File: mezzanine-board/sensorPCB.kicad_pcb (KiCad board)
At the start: 2 copper layers, 55.5 x 19.8 mm, 21 parts, among them J1 90152-2140, U3 AS72652, U4 AS72653, U6 AS72651

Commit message: Add TE 215307-7 connector to mezzanine libraries
Import the Library Loader part (14-pin TE Connectivity connector) into
the mezzanine's already-registered SamacSys_Parts library: footprint, 3D
model, and symbol appended. 3D path rewritten to ${KIPRJMOD}-relative and
the symbol's Footprint property qualified with the library nickname.
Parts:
- removed J1: 90152-2140, SamacSys_Parts:901522140
- added J2: SSQ-120-04-G-D, SamacSys_Parts:SSQ-120-XX-YYY-D, F.Cu at (171.7, 92.0)
- moved U3 2.92 mm to (146.8, 83.2)
- moved U4 2.92 mm to (154.4, 83.2)
- moved U6 2.92 mm to (139.2, 83.2)
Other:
- board size 55.5 x 19.8 mm -> 55.5 x 16.6 mm

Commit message: Add Molex 90122-0770 right-angle header to main board libraries
Import the Library Loader part (2x10 right-angle header, 20-pin) into the
main board's SamacSys_Parts library: footprint, 3D model, and symbol
appended. 3D path rewritten to ${KIPRJMOD}-relative and the symbol's
Footprint property qualified with the library nickname.
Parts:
- moved U6 42.8 mm to (97.3, 91.6)
- moved U3 42.3 mm to (105.4, 91.7)
- moved U4 41.6 mm to (113.8, 91.9)
- moved J2 1.95 mm to (171.7, 94.0)
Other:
- board size 55.5 x 16.6 mm -> 82.1 x 13.6 mm
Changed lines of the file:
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@@
 	(footprint "SamacSys_Parts:AS72651BLGT"
 		(layer "F.Cu")
-		(at 146.791 83.165)
+		(at 105.41 91.694)
 		(descr "LGA-20")
 		(tags "Integrated Circuit")
@@
 	(footprint "SamacSys_Parts:SSQ-120-XX-YYY-D"
 		(layer "F.Cu")
-		(at 171.704 92.0295)
+		(at 171.704 93.98)
 		(descr "SSQ-120-XX-YYY-D")
 		(tags "Connector")
@@
 	(footprint "SamacSys_Parts:AS72651BLGT"
 		(layer "F.Cu")
-		(at 154.411 83.165)
+		(at 113.792 91.948)
 		(descr "LGA-20")
 		(tags "Integrated Circuit")
@@
 	(footprint "SamacSys_Parts:AS72651BLGT"
 		(layer "F.Cu")
-		(at 139.171 83.165)
+		(at 97.254 91.582)
 		(descr "LGA-20")
 		(tags "Integrated Circuit")
@@
 	)
 	(gr_rect
-		(start 119.834322 78.994)
+		(start 93.218 82.042)
 		(end 175.316821 95.60057)
 		(stroke

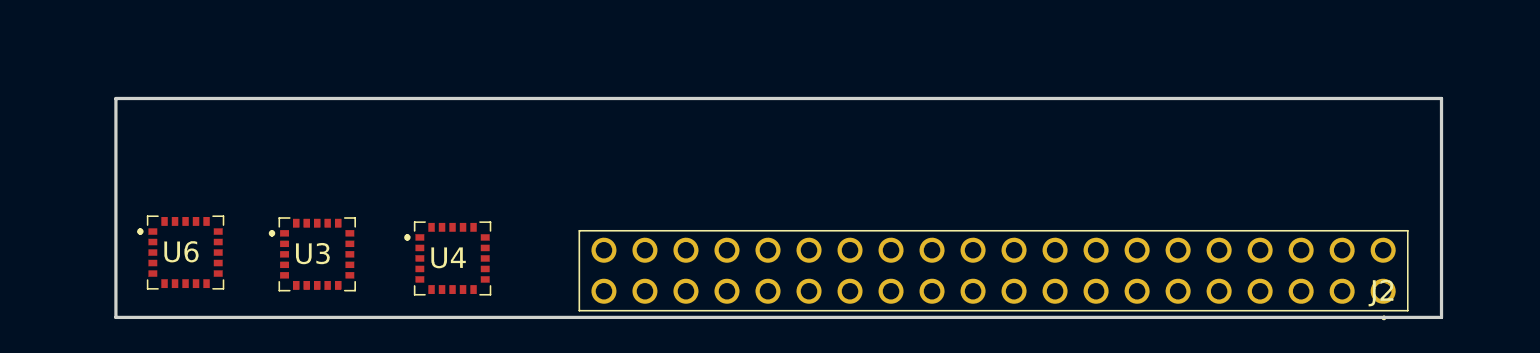
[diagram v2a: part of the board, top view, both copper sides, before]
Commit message: Add Samtec FTSH-110-01-F-D-RA header to mezzanine libraries
Import the Library Loader part (2x10 right-angle 1.27mm fine-pitch header)
into the mezzanine's SamacSys_Parts library: footprint, 3D model, and
symbol appended. 3D path rewritten to ${KIPRJMOD}-relative and the
symbol's Footprint property qualified with the library nickname.
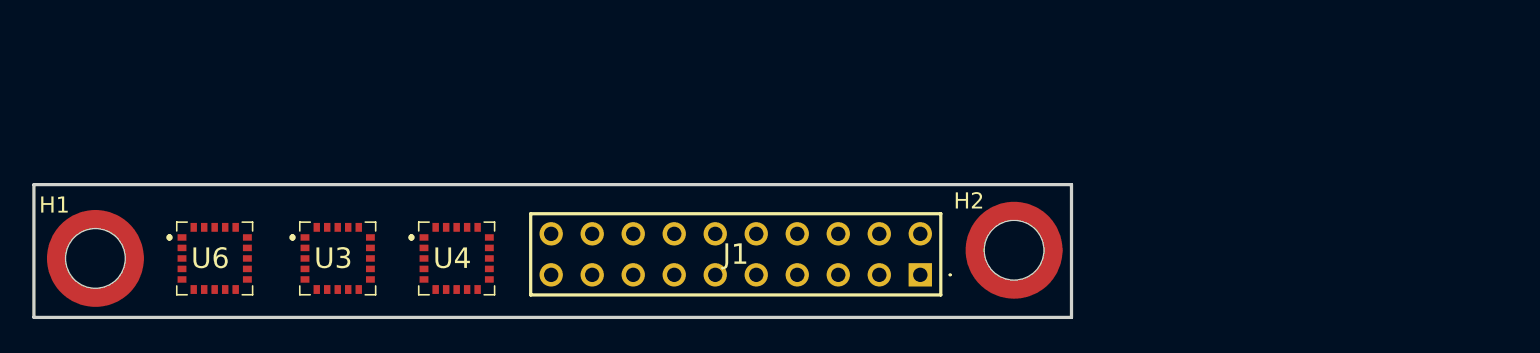
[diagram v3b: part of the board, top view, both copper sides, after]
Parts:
- removed J2: SSQ-120-04-G-D, SamacSys_Parts:SSQ-120-XX-YYY-D
- added H1: MountingHole, Mounting_Wuerth:Mounting_Wuerth_WA-SMSI-M2.5_H0.5mm_9774005151, F.Cu at (91.9, 91.9)
- added H2: MountingHole, Mounting_Wuerth:Mounting_Wuerth_WA-SMSI-M2.5_H0.5mm_9774005151, F.Cu at (148.8, 91.4)
- added J1: 1-534998-0, SamacSys_Parts:15349980, F.Cu at (143.0, 93.0)
- moved U6 1.84 mm to (99.1, 91.9)
- moved U3 1.30 mm to (106.7, 91.9)
- moved U4 0.25 mm to (114.0, 91.9)
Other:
- board size 82.1 x 13.6 mm -> 64.3 x 8.2 mm

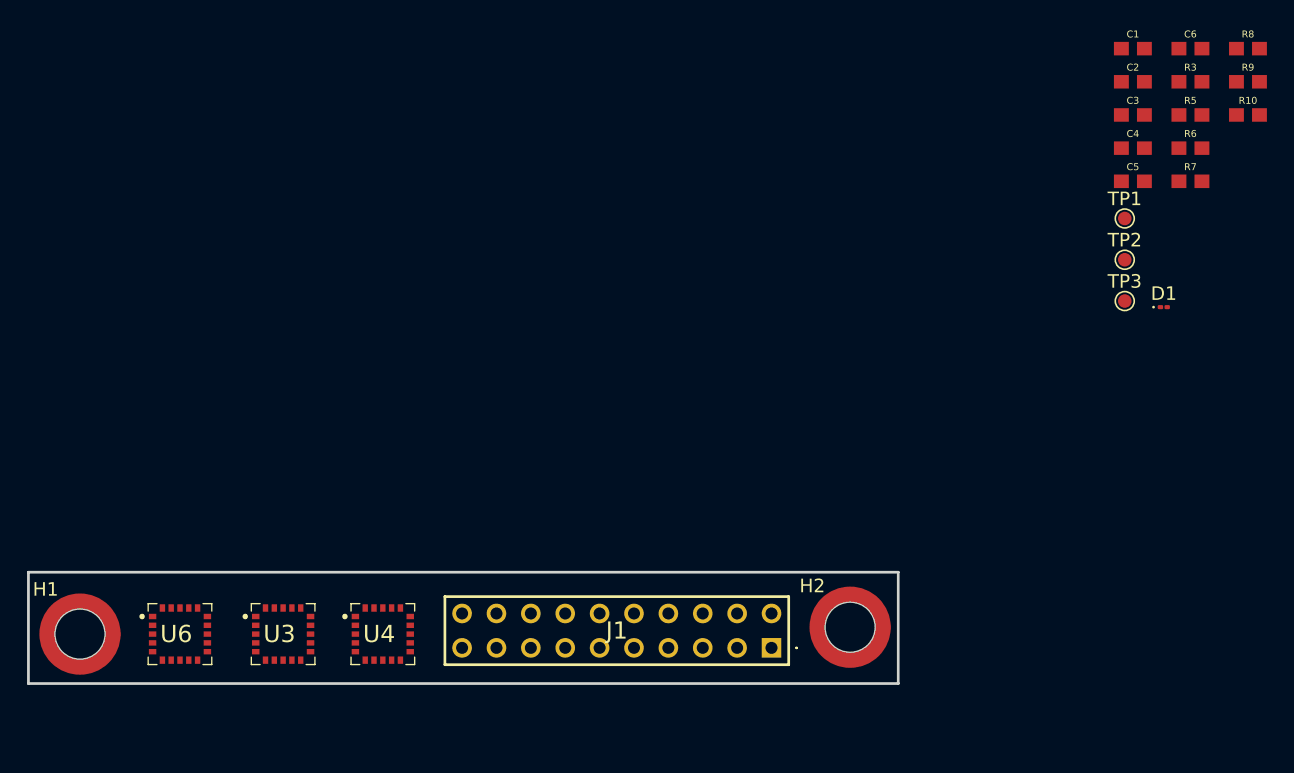
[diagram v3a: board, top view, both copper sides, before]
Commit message: Add Amphenol 20021311-00020T4LF (Minitek127) to mezzanine libraries
Import the Library Loader part (20-pin 1.27mm board-to-board connector)
into the mezzanine's SamacSys_Parts library: footprint, 3D model, and
symbol appended. 3D path rewritten to ${KIPRJMOD}-relative and the
symbol's Footprint property qualified with the library nickname.
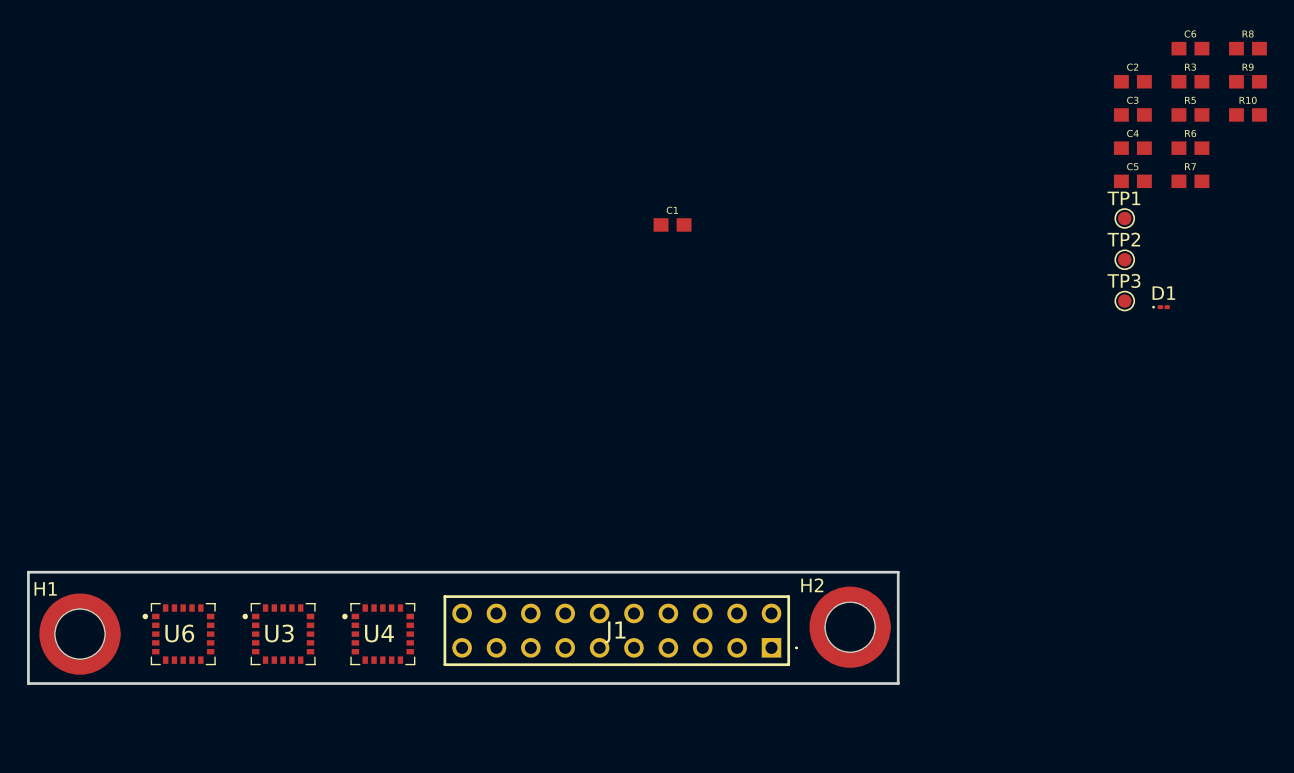
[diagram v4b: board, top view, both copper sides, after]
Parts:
- moved C1 36.4 mm to (135.7, 61.7)
- moved U6 0.24 mm to (99.3, 91.9)
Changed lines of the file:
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@@
 		(model "${KIPRJMOD}/libraries/3dmodels/SamacSys_Parts.3dshapes/1-534998-0.stp"
 			(offset
-				(xyz -11.43000013 1.269999962 0.4900000022)
+				(xyz -11.43 1.27 -1.51)
 			)
 			(scale
@@
 			)
 			(rotate
-				(xyz 0 0 0)
+				(xyz -0 -180 -0)
 			)
 		)
@@
 	(footprint "SamacSys_Parts:AS72651BLGT"
 		(layer "F.Cu")
-		(at 99.06 91.948)
+		(at 99.3 91.948)
 		(descr "LGA-20")
 		(tags "Integrated Circuit")
@@
 	(footprint "SparkfunLibrary:0603"
 		(layer "F.Cu")
-		(at 169.7343 48.6933)
+		(at 135.724 61.722)
 		(descr "Generic 1608 (0603) package\n\n0.2mm courtyard excess rounded to nearest 0.05mm.")
 		(property "Reference" "C1"

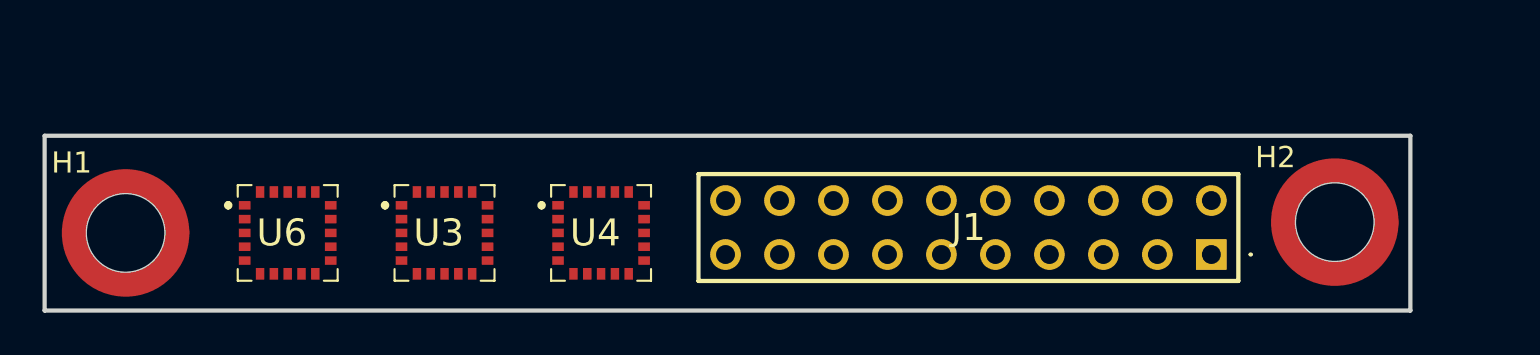
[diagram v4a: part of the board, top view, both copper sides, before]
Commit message: Add Samtec FTSH-110-01-F-D-RA header to main board libraries
Import the Library Loader part (2x10 right-angle 1.27mm fine-pitch header)
into the main board's SamacSys_Parts library: footprint, 3D model, and
symbol appended. 3D path rewritten to ${KIPRJMOD}-relative and the
symbol's Footprint property qualified with the library nickname.
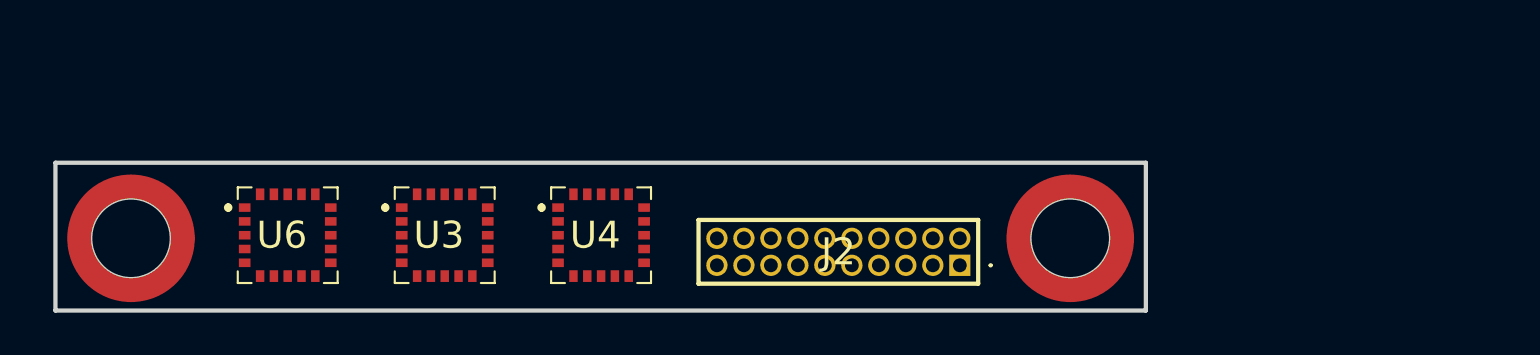
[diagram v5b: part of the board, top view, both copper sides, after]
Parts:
- removed J1: 1-534998-0, SamacSys_Parts:15349980
- added J2: 20021311-00020T4LF, SamacSys_Parts:2002131100020T4LF, F.Cu at (131.2, 93.5)
- moved H2 12.5 mm to (136.4, 92.2)
- moved H1 0.36 mm to (92.2, 92.2)
- moved U3 0.11 mm to (106.7, 92.1)
- moved U4 0.11 mm to (114.0, 92.1)
- moved U6 0.11 mm to (99.3, 92.1)
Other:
- board size 64.3 x 8.2 mm -> 51.3 x 7 mm

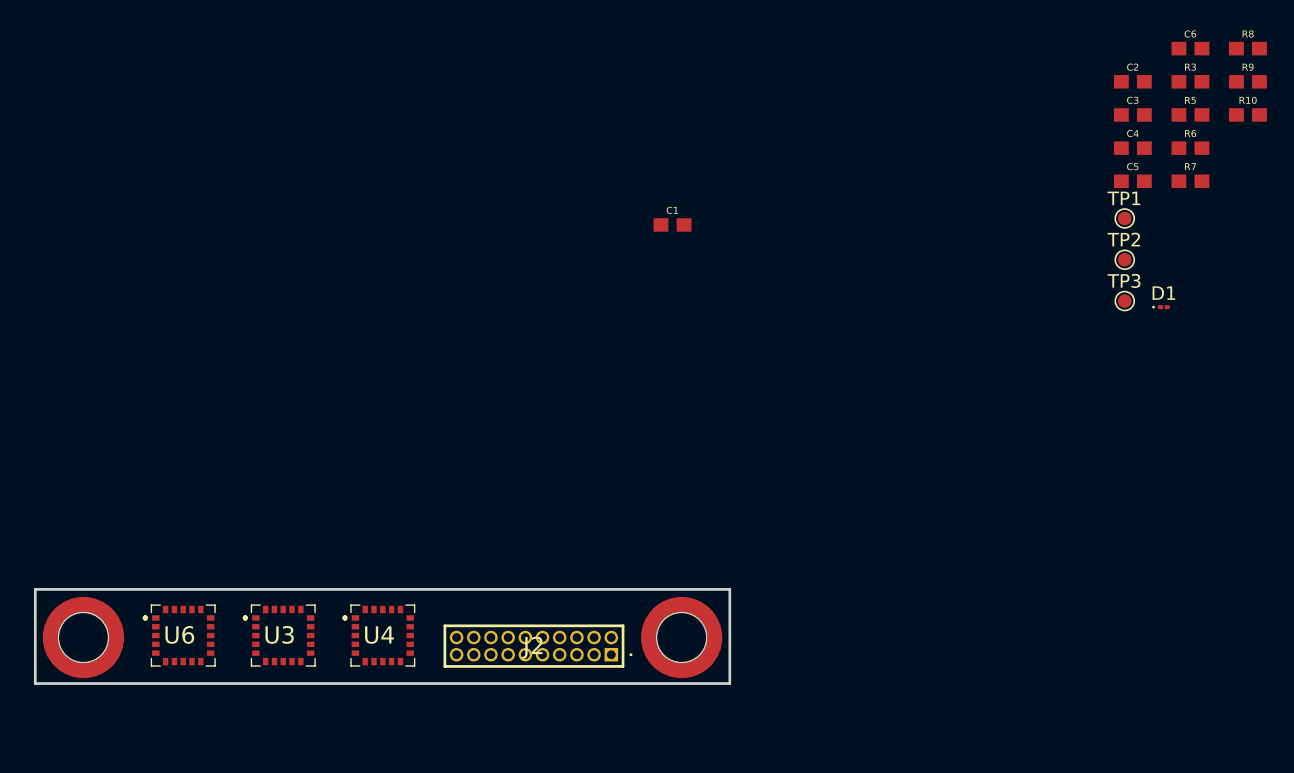
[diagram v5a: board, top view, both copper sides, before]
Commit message: Add Samtec FTSH-105-04-L-D-RA and SFMC-105-01-L-D to both boards
Import two Library Loader parts (a 2x5 1.27mm right-angle header and its
mating 2x5 socket strip) into the SamacSys_Parts library of BOTH the main
board and the mezzanine board: footprints, 3D models, and symbols
appended. 3D paths rewritten to ${KIPRJMOD}-relative and each symbol's
Footprint property qualified with the library nickname.
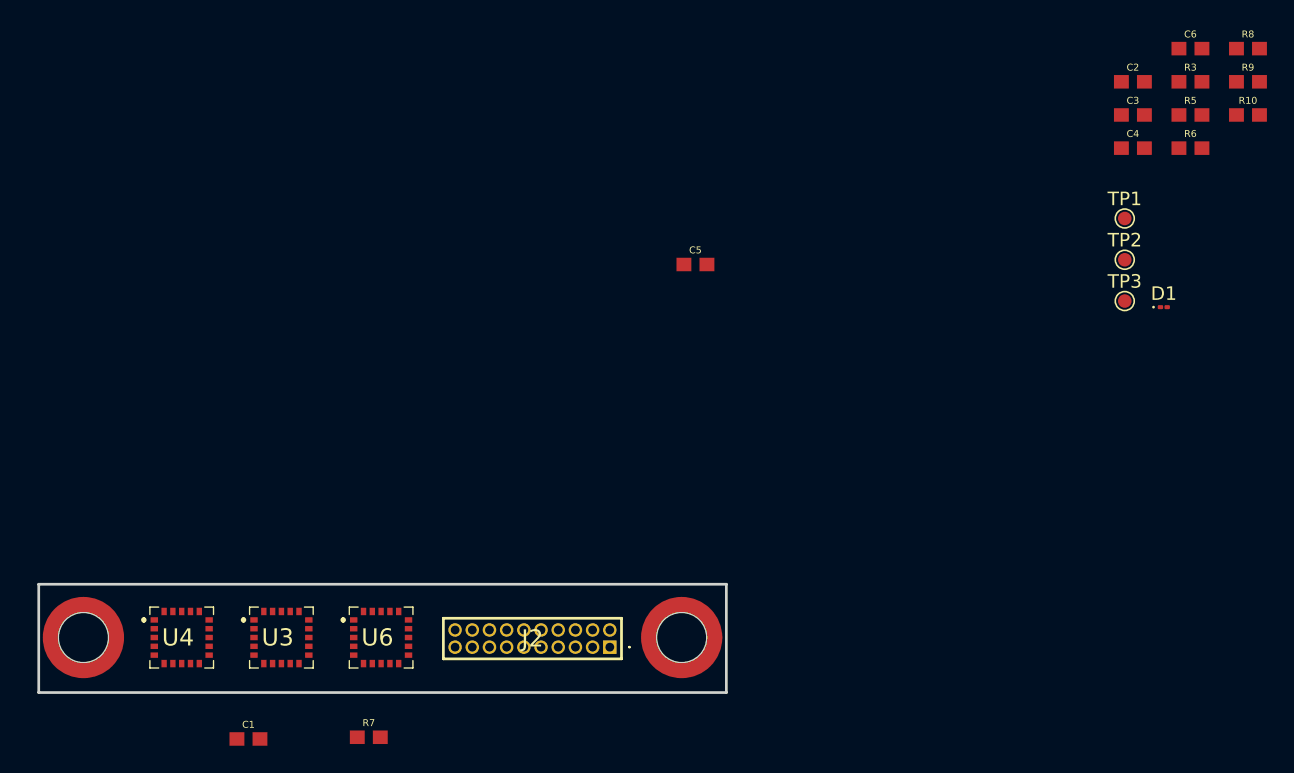
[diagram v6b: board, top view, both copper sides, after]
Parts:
- moved R7 73.3 mm to (113.3, 99.6)
- moved C1 49.2 mm to (104.4, 99.7)
- moved C5 32.9 mm to (137.4, 64.6)
- moved U4 14.9 mm to (99.2, 92.2)
- moved U6 14.6 mm to (113.9, 92.2)
- moved J2 0.57 mm to (131.1, 92.9)
- moved U3 0.20 mm to (106.6, 92.2)
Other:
- board size 51.3 x 7 mm -> 50.8 x 8 mm
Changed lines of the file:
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@@
 		)
 		(property "Value" "MountingHole"
-			(at 0 3.95 0)
+			(at 0 6.096 0)
 			(layer "F.Fab")
 			(effects
@@
 	(footprint "SamacSys_Parts:AS72651BLGT"
 		(layer "F.Cu")
-		(at 106.689 92.055)
+		(at 106.553 92.202)
 		(descr "LGA-20")
 		(tags "Integrated Circuit")
@@
 	(footprint "SamacSys_Parts:AS72651BLGT"
 		(layer "F.Cu")
-		(at 114.046 92.055)
+		(at 99.187 92.202)
 		(descr "LGA-20")
 		(tags "Integrated Circuit")
@@
 	(footprint "SparkfunLibrary:0603"
 		(layer "F.Cu")
-		(at 169.7343 58.4965)
+		(at 137.414 64.643)
 		(descr "Generic 1608 (0603) package\n\n0.2mm courtyard excess rounded to nearest 0.05mm.")
 		(property "Reference" "C5"
@@
 	(footprint "SparkfunLibrary:0603"
 		(layer "F.Cu")
-		(at 173.9851 58.4965)
+		(at 113.284 99.568)
 		(descr "Generic 1608 (0603) package\n\n0.2mm courtyard excess rounded to nearest 0.05mm.")
 		(property "Reference" "R7"
@@
 	(footprint "SamacSys_Parts:AS72651BLGT"
 		(layer "F.Cu")
-		(at 99.3 92.055)
+		(at 113.919 92.202)
 		(descr "LGA-20")
 		(tags "Integrated Circuit")
@@
 	(footprint "SparkfunLibrary:0603"
 		(layer "F.Cu")
-		(at 135.724 61.722)
+		(at 104.394 99.695)
 		(descr "Generic 1608 (0603) package\n\n0.2mm courtyard excess rounded to nearest 0.05mm.")
 		(property "Reference" "C1"
@@
 	)
 	(footprint "SamacSys_Parts:2002131100020T4LF"
+		(locked yes)
 		(layer "F.Cu")
-		(at 131.201 93.472)
+		(at 131.0894 92.9132)
 		(descr "20021311-00020T4LF-2")
 		(tags "Connector")
@@
 	)
 	(gr_rect
-		(start 88.646 88.646)
-		(end 139.953999 95.60057)
+		(start 88.9 88.265)
+		(end 139.699999 96.266)
 		(stroke
 			(width 0.2)
-			(type default)
+			(type solid)
 		)
 		(fill no)
+		(locked yes)
 		(layer "Edge.Cuts")
 	)
